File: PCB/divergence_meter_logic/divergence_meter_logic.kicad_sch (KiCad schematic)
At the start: 66 parts, among them J1 Conn_Coaxial_Power, Q1 BC547, Q10 BC547, Q11 BC547, Q12 BC547, Q13 BC547, Q14 BC547, Q15 BC547, Q16 BC547, Q2 BC547, Q3 BC547, Q4 BC547, Q5 BC547, Q6 BC547, Q7 BC547, Q8 BC547, Q9 BC547, SW1 SW_Push, SW2 SW_Push, SW3 SW_Push

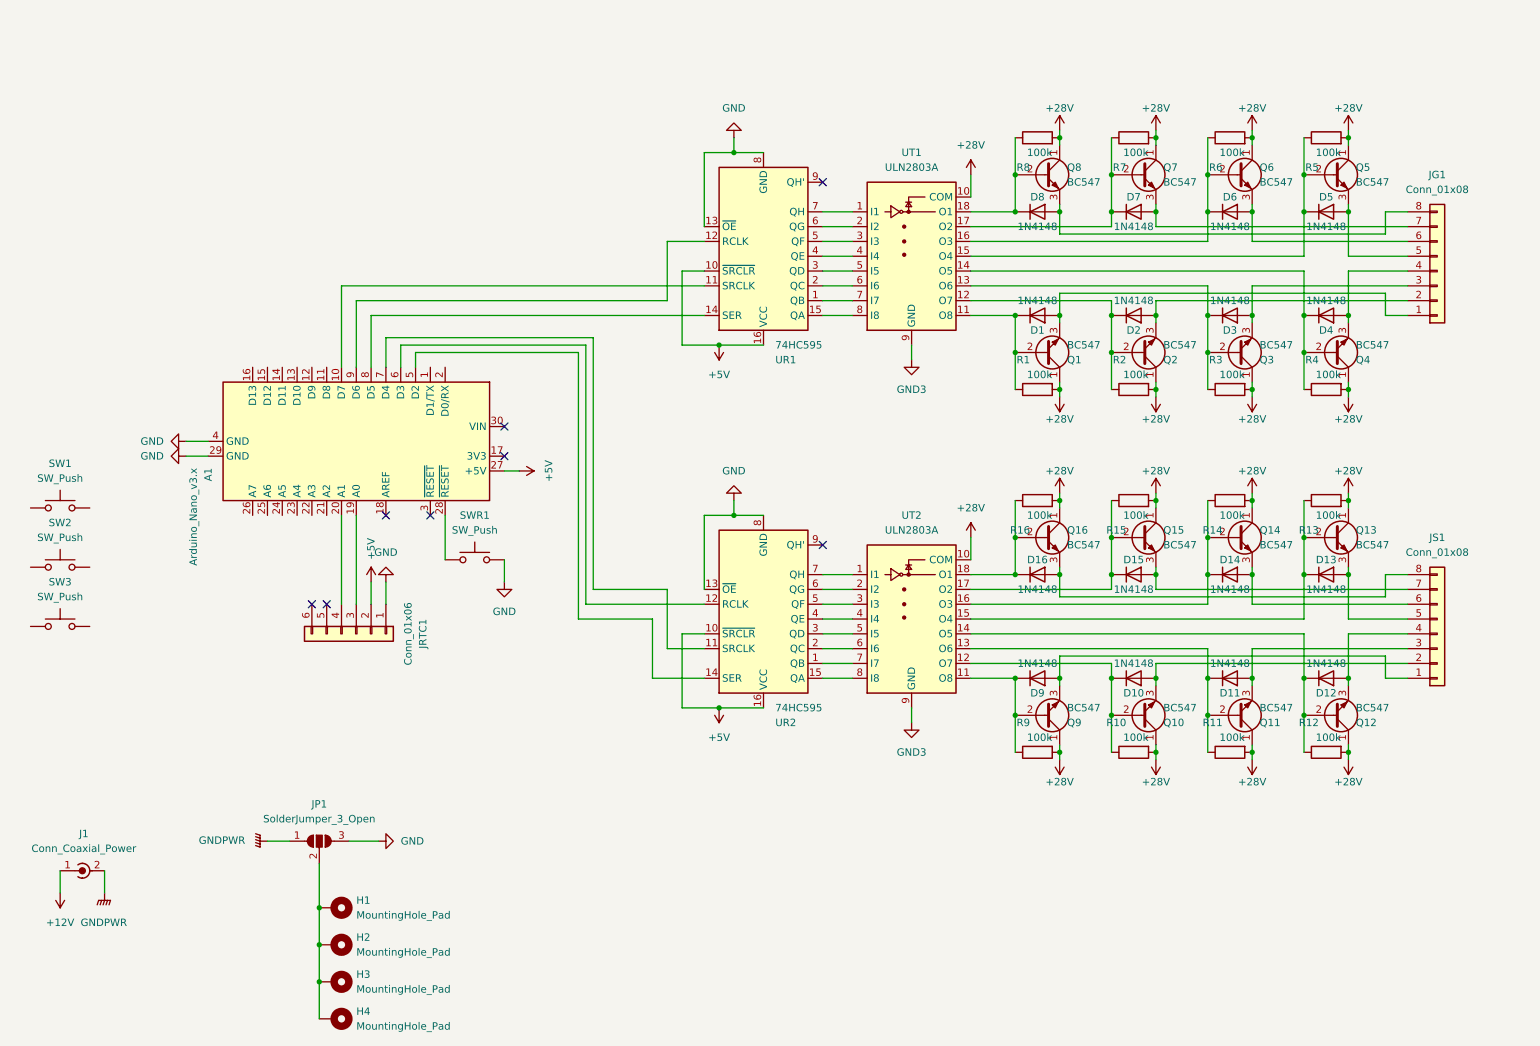
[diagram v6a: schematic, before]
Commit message: logic pcb almost finished, remaking top
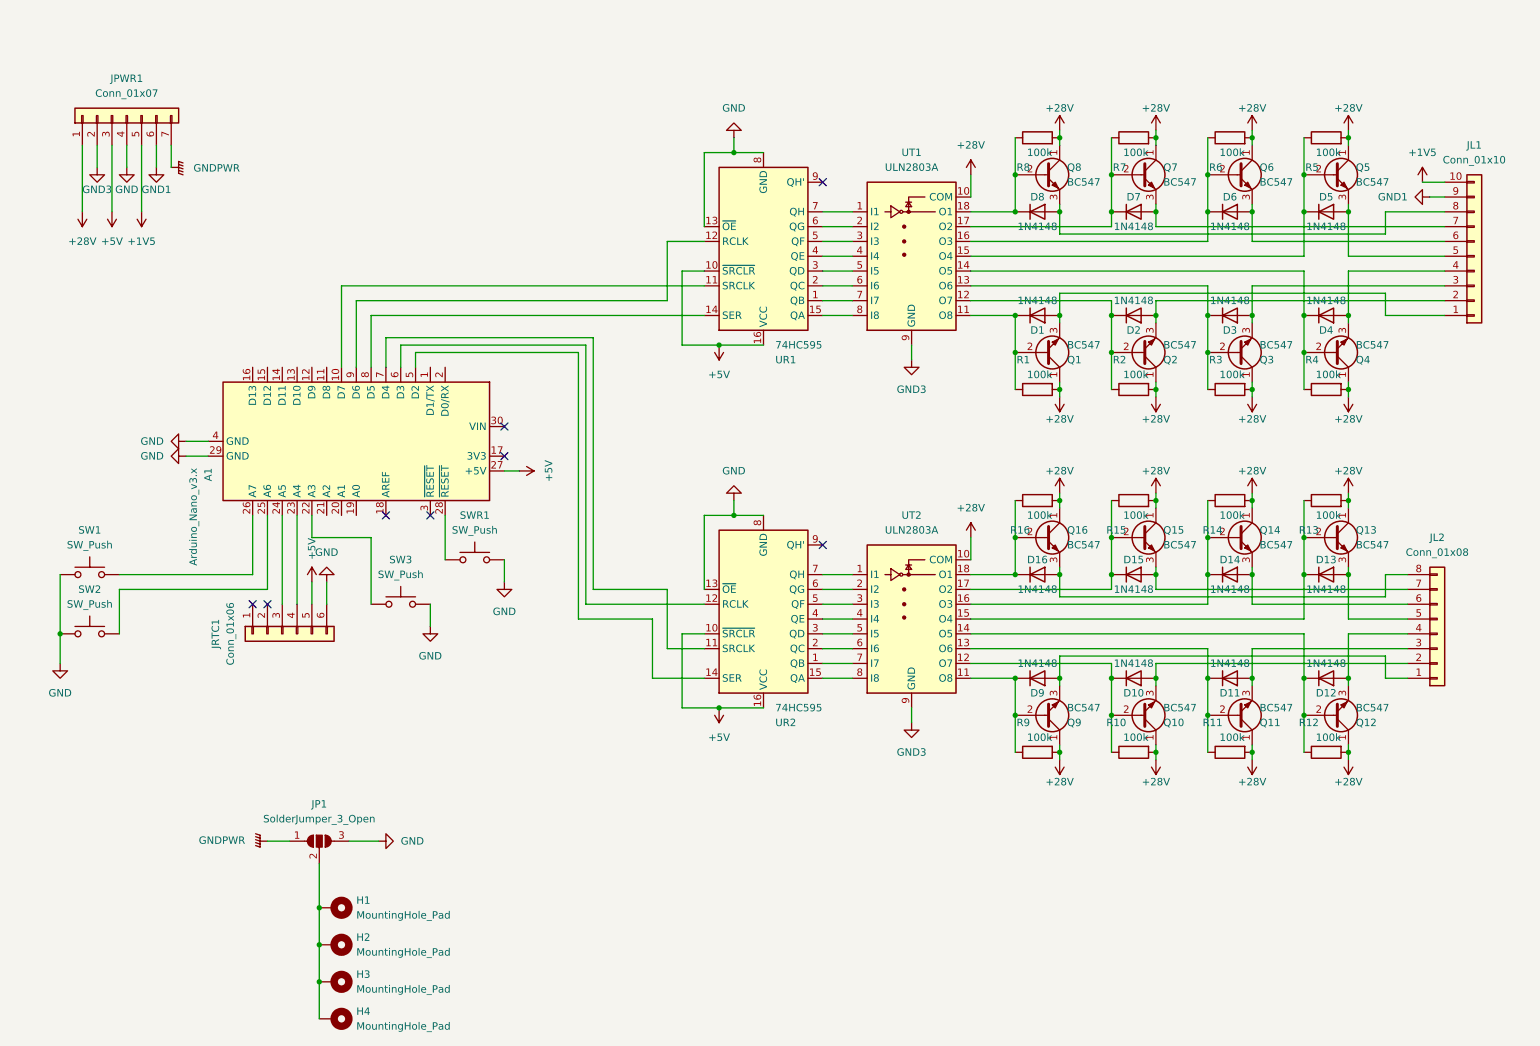
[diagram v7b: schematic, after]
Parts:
- removed J1: Conn_Coaxial_Power, symbol Connector:Conn_Coaxial_Power
- removed JG1: Conn_01x08, Connector_PinSocket_2.54mm:PinSocket_1x08_P2.54mm_Vertical, symbol Connector_Generic:Conn_01x08
- added JL1: Conn_01x10, Connector_PinSocket_2.54mm:PinSocket_1x10_P2.54mm_Vertical, symbol Connector_Generic:Conn_01x10
- added JPWR1: Conn_01x07, Connector_PinHeader_2.54mm:PinHeader_1x07_P2.54mm_Horizontal, symbol Connector_Generic:Conn_01x07
- SW1, SW2, SW3, SWR1: footprint (none) -> Button_Switch_THT:SW_PUSH_6mm_H4.3mm
- renumbered JS1 to JL2
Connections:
- net +28V: now also JPWR1.1 (Pin_1)
- net +5V: now also JRTC1.5 (Pin_5), JPWR1.3 (Pin_3); no longer JRTC1.2 (Pin_2)
- net GND: now also JRTC1.6 (Pin_6), SW1.1, SW2.1, SW3.2, JPWR1.4 (Pin_4); no longer JRTC1.1 (Pin_1)
- net GND3: now also JPWR1.2 (Pin_2)
- net GNDPWR: now also JPWR1.7 (Pin_7)
- net at D2.2 (A), Q2.3 (E): now also JL1.2 (Pin_2)
- net at D8.2 (A), Q8.3 (E): now also JL1.8 (Pin_8)
- net at A1.19 (A0): no longer JRTC1.3 (Pin_3)
- net at A1.20 (A1): no longer JRTC1.4 (Pin_4)
- net at A1.22 (A3): now also SW3.1
- net at A1.23 (A4): now also JRTC1.4 (Pin_4)
- net at A1.24 (A5): now also JRTC1.3 (Pin_3)
- net at A1.25 (A6): now also SW2.2
- net at A1.26 (A7): now also SW1.2
- net at D4.2 (A), Q4.3 (E): now also JL1.4 (Pin_4)
- net at D7.2 (A), Q7.3 (E): now also JL1.7 (Pin_7)
- net at D3.2 (A), Q3.3 (E): now also JL1.3 (Pin_3)
- net at D1.2 (A), Q1.3 (E): now also JL1.1 (Pin_1)
- net at D5.2 (A), Q5.3 (E): now also JL1.5 (Pin_5)
- net at D6.2 (A), Q6.3 (E): now also JL1.6 (Pin_6)
- new net +1V5: JL1.10 (Pin_10), JPWR1.5 (Pin_5)
- new net GND1: JL1.9 (Pin_9), JPWR1.6 (Pin_6)
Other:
- moved on the sheet: SW1, SW2, SW3

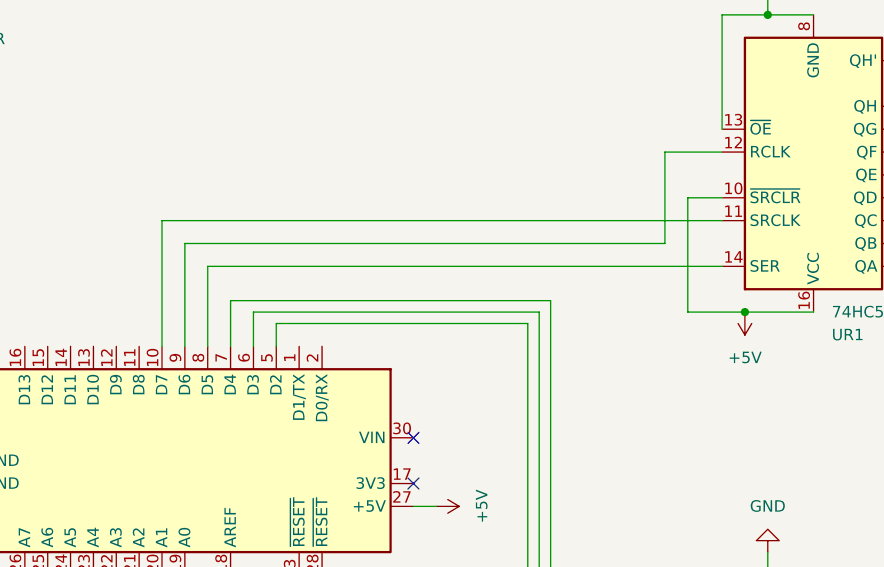
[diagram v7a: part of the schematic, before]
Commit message: top done, logic almost
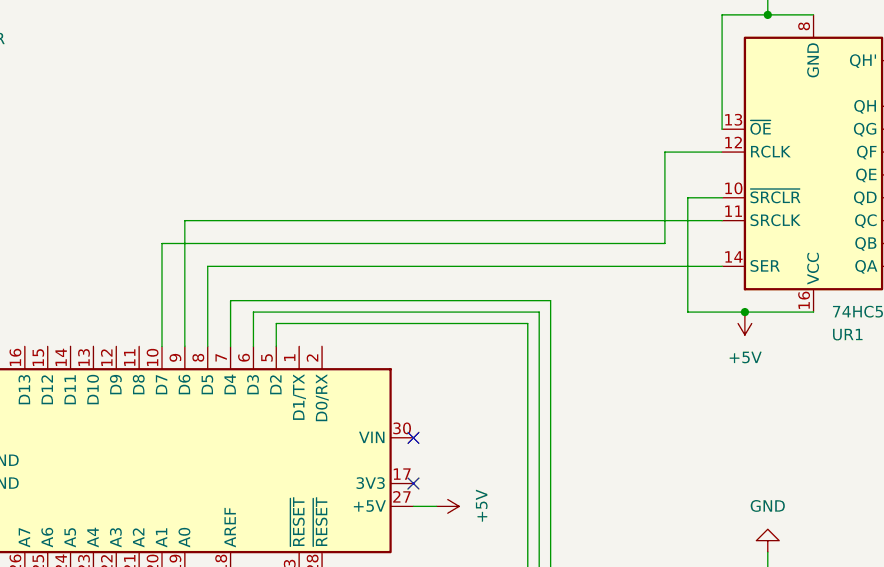
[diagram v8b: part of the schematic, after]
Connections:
- net at UR1.11 (SRCLK): now also A1.9 (D6); no longer A1.10 (D7)
- net at UR1.12 (RCLK): now also A1.10 (D7); no longer A1.9 (D6)
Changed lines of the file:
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@@
-    (stroke (width 0) (type default) (color 0 0 0 0))
-  )
-  (wire (pts (xy 73.66 60.96) (xy 135.89 60.96))
     (stroke (width 0) (type default) (color 0 0 0 0))
   )
@@
     (stroke (width 0) (type default) (color 0 0 0 0))
   )
+  (wire (pts (xy 76.2 60.96) (xy 76.2 74.93))
+    (stroke (width 0) (type default) (color 0 0 0 0))
+  )
   (wire (pts (xy 181.61 110.49) (xy 189.23 110.49))
     (stroke (width 0) (type default) (color 0 0 0 0))
@@
     (stroke (width 0) (type default) (color 0 0 0 0))
   )
-  (wire (pts (xy 73.66 74.93) (xy 73.66 60.96))
-    (stroke (width 0) (type default) (color 0 0 0 0))
-  )
   (wire (pts (xy 115.57 115.57) (xy 135.89 115.57))
     (stroke (width 0) (type default) (color 0 0 0 0))
@@
     (stroke (width 0) (type default) (color 0 0 0 0))
   )
+  (wire (pts (xy 135.89 60.96) (xy 76.2 60.96))
+    (stroke (width 0) (type default) (color 0 0 0 0))
+  )
   (wire (pts (xy 29.21 36.83) (xy 29.21 48.26))
     (stroke (width 0) (type default) (color 0 0 0 0))
@@
     (stroke (width 0) (type default) (color 0 0 0 0))
   )
-  (wire (pts (xy 76.2 74.93) (xy 76.2 63.5))
-    (stroke (width 0) (type default) (color 0 0 0 0))
-  )
   (wire (pts (xy 181.61 60.96) (xy 222.25 60.96))
     (stroke (width 0) (type default) (color 0 0 0 0))
@@
     (stroke (width 0) (type default) (color 0 0 0 0))
   )
-  (wire (pts (xy 76.2 63.5) (xy 129.54 63.5))
+  (wire (pts (xy 73.66 63.5) (xy 129.54 63.5))
     (stroke (width 0) (type default) (color 0 0 0 0))
   )
   (wire (pts (xy 83.82 74.93) (xy 83.82 71.12))
+    (stroke (width 0) (type default) (color 0 0 0 0))
+  )
+  (wire (pts (xy 73.66 63.5) (xy 73.66 74.93))
     (stroke (width 0) (type default) (color 0 0 0 0))
   )
@@
   (symbol (lib_id "power:+1V5") (at 259.08 43.18 0) (unit 1)
     (in_bom yes) (on_board yes) (fields_autoplaced)
-    (property "Reference" "#PWR?" (id 0) (at 259.08 46.99 0)
+    (property "Reference" "#PWR0124" (id 0) (at 259.08 46.99 0)
       (effects (font (size 1.27 1.27)) hide)
     )
@@
   (symbol (lib_id "power:GND1") (at 260.35 45.72 270) (unit 1)
     (in_bom yes) (on_board yes) (fields_autoplaced)
-    (property "Reference" "#PWR?" (id 0) (at 254 45.72 0)
+    (property "Reference" "#PWR0123" (id 0) (at 254 45.72 0)
       (effects (font (size 1.27 1.27)) hide)
     )
@@
       (reference "#PWR0122") (unit 1) (value "GND") (footprint "")
     )
+    (path "/80a6cf06-d5d7-4c05-addd-ebf6c16f8a92"
+      (reference "#PWR0123") (unit 1) (value "GND1") (footprint "")
+    )
     (path "/3c95c987-57df-4080-b48a-299923ebd797"
-      (reference "#PWR?") (unit 1) (value "+1V5") (footprint "")
-    )
-    (path "/80a6cf06-d5d7-4c05-addd-ebf6c16f8a92"
-      (reference "#PWR?") (unit 1) (value "GND1") (footprint "")
+      (reference "#PWR0124") (unit 1) (value "+1V5") (footprint "")
     )
     (path "/1cd08355-701e-4fba-886f-d48517dcccf5"
